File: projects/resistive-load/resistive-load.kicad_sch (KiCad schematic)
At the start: 7 parts, among them J1 MicroFit_V_2, J2 redcude_7461166, J3 redcude_7461166, J4 redcude_7461166, J8 Barrel_jack

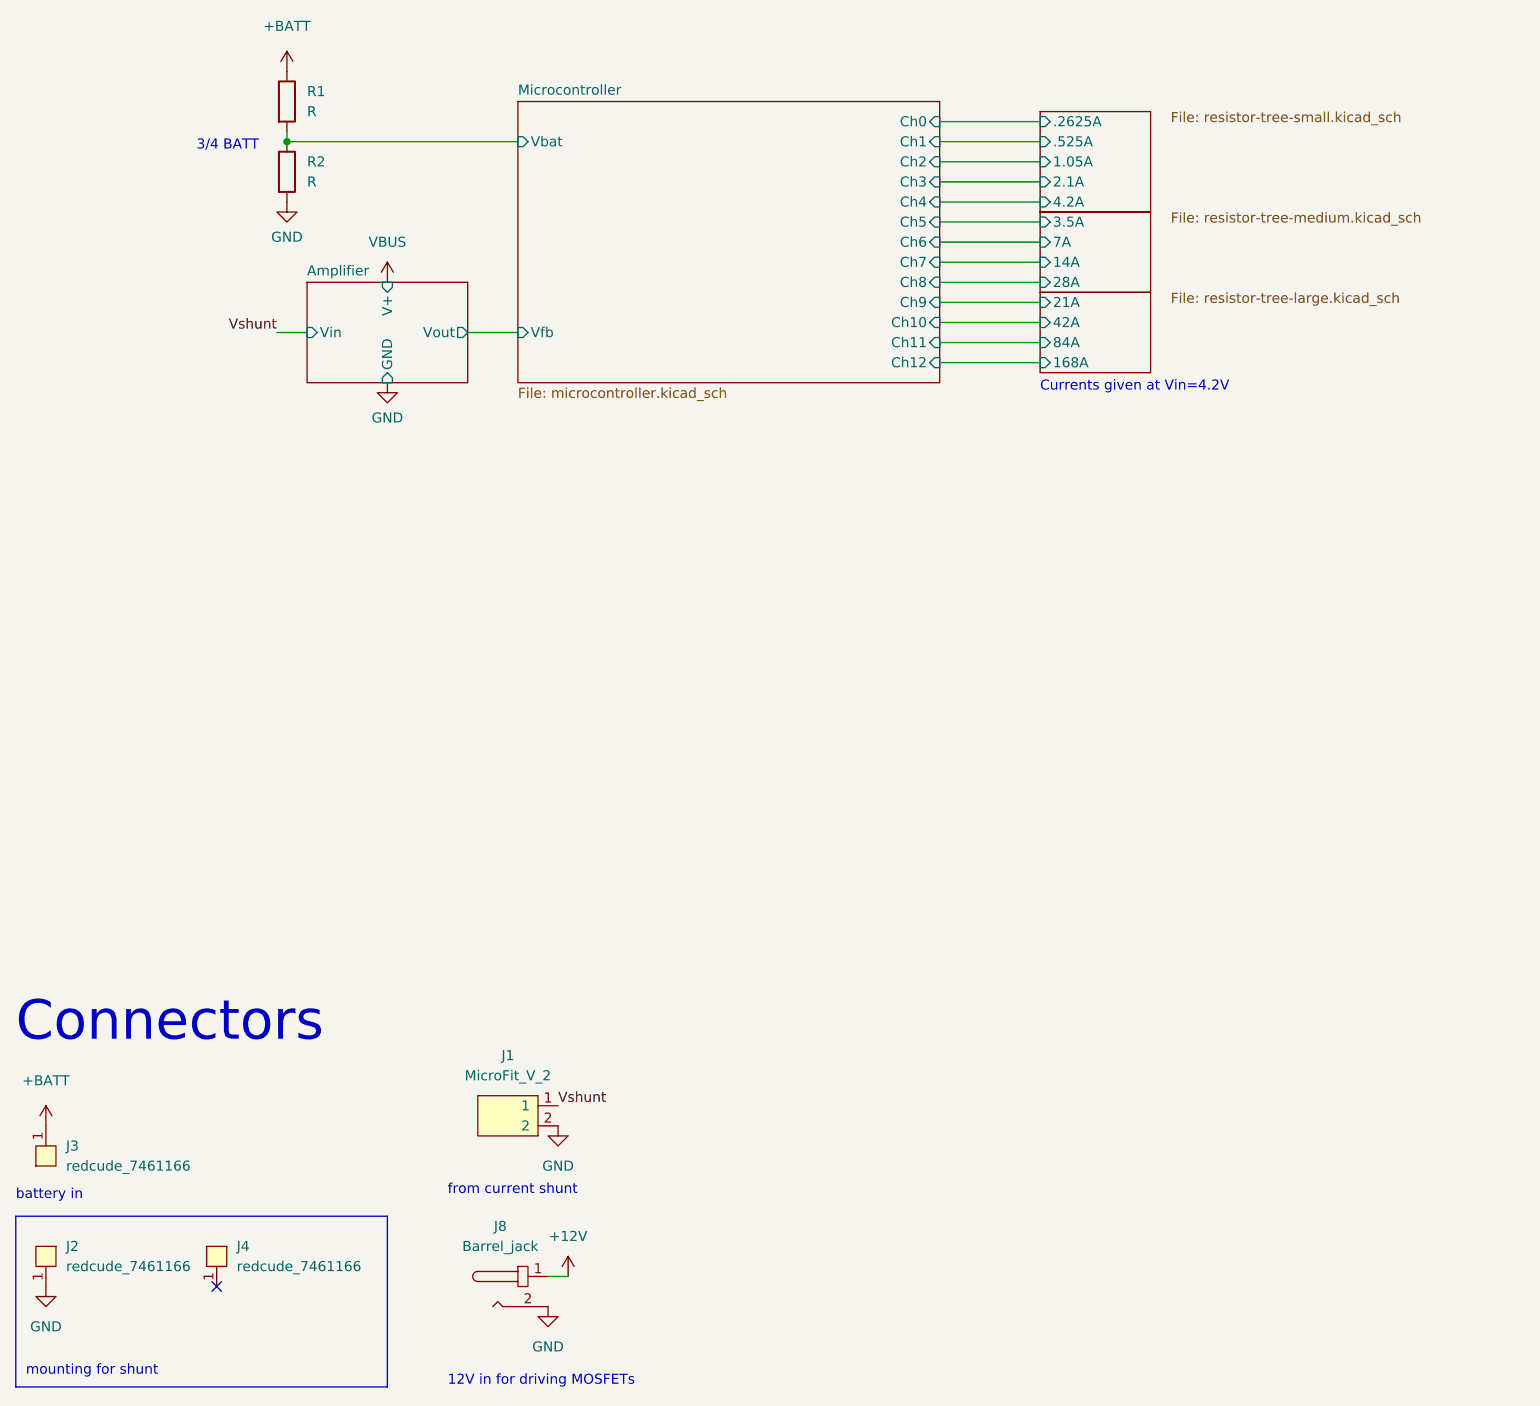
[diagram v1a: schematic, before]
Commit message: fix: update pin assignment for transistors
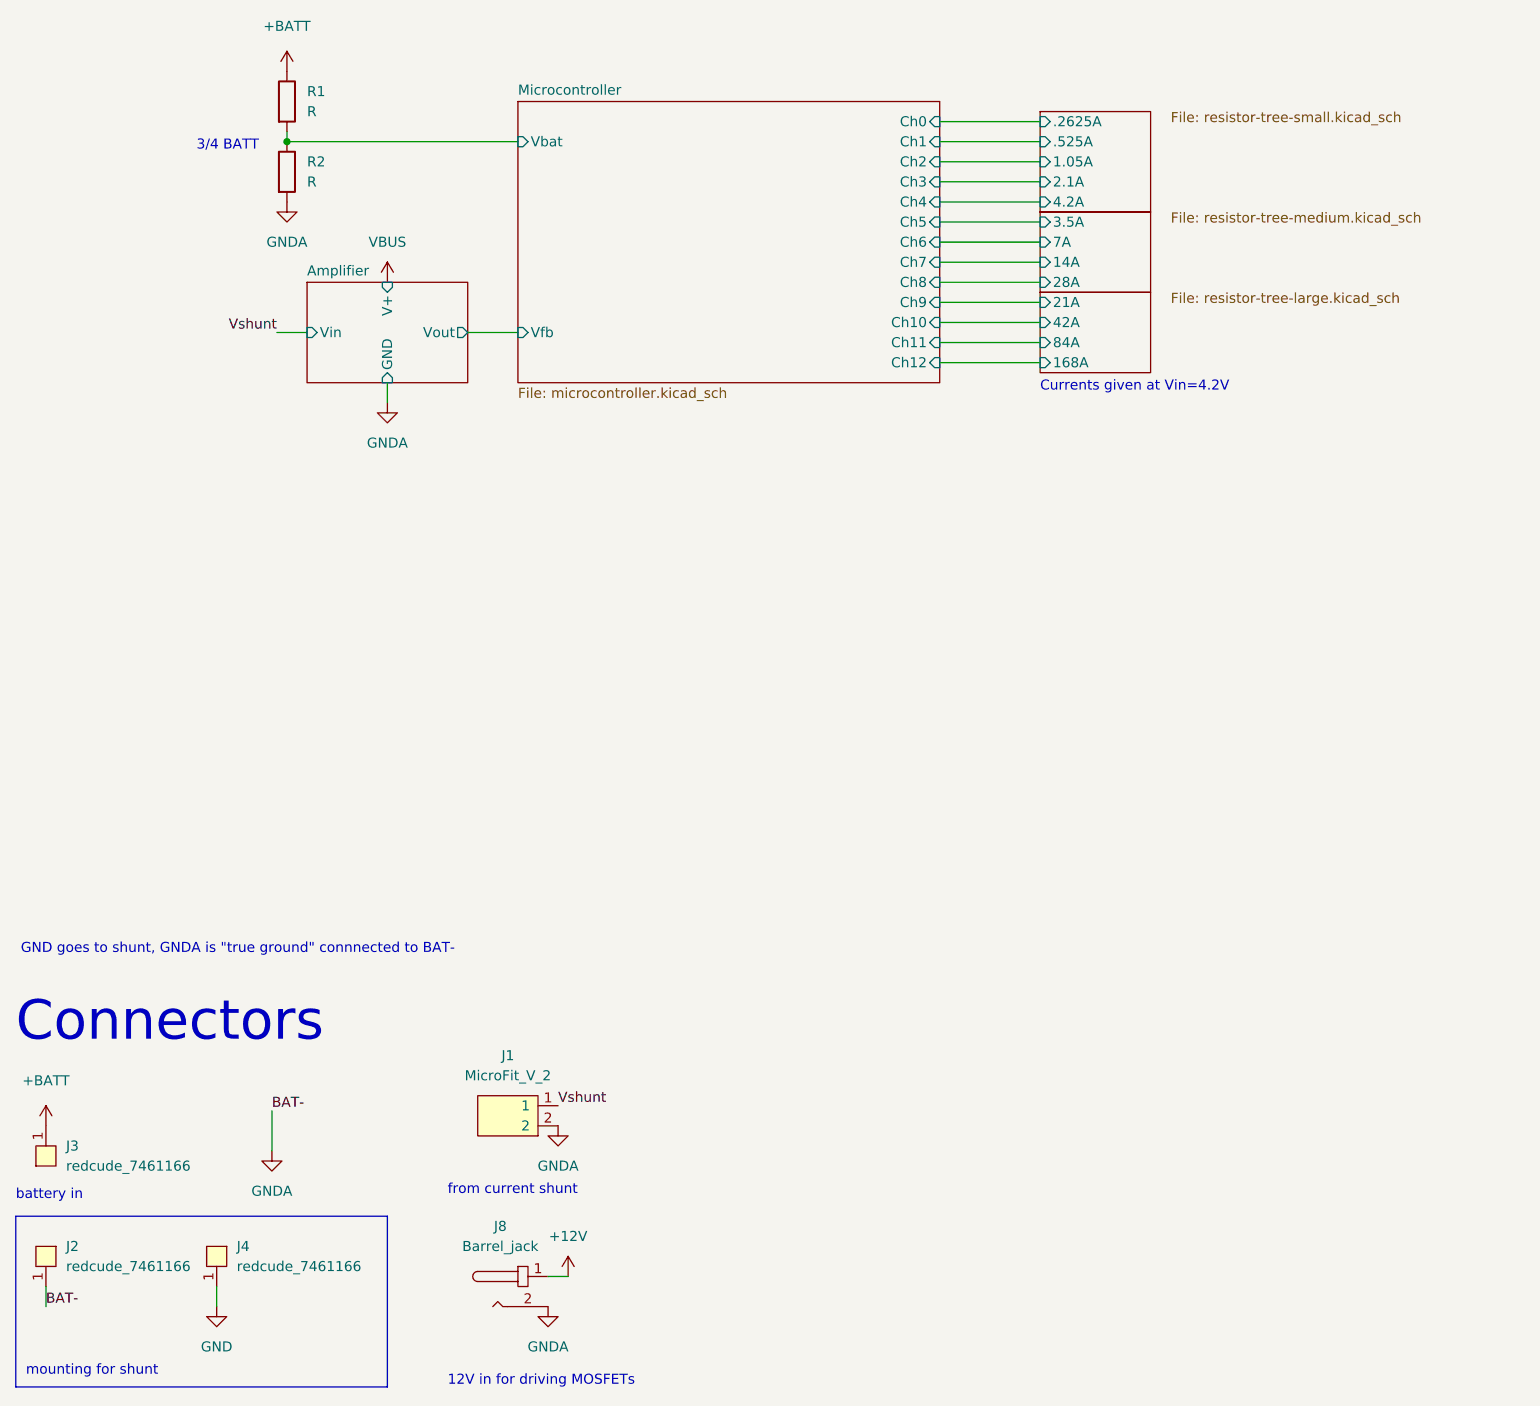
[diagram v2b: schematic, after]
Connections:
- net GND: now also J4.1; no longer J1.2, J2.1, J8.2 (Shell), R2.2
- new net GNDA: J1.2, J2.1, J8.2 (Shell), R2.2
- no-connect marks 1 -> 0
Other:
- note added: "GND goes to shunt, GNDA is "true ground" connnected to BAT-"
